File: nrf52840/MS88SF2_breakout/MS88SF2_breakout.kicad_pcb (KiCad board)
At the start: 2 copper layers, 1 part, among them U1 MS88SF2

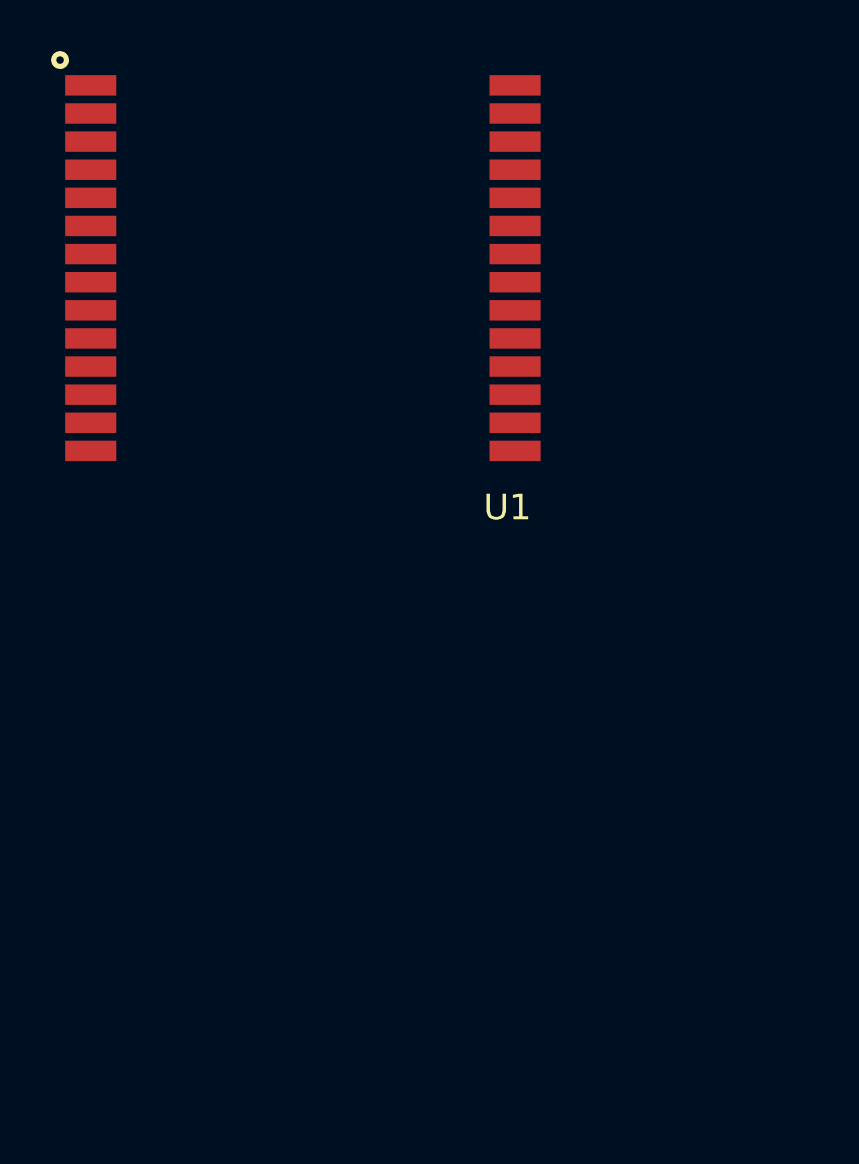
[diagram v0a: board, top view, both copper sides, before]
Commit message: nrf5: Start routing
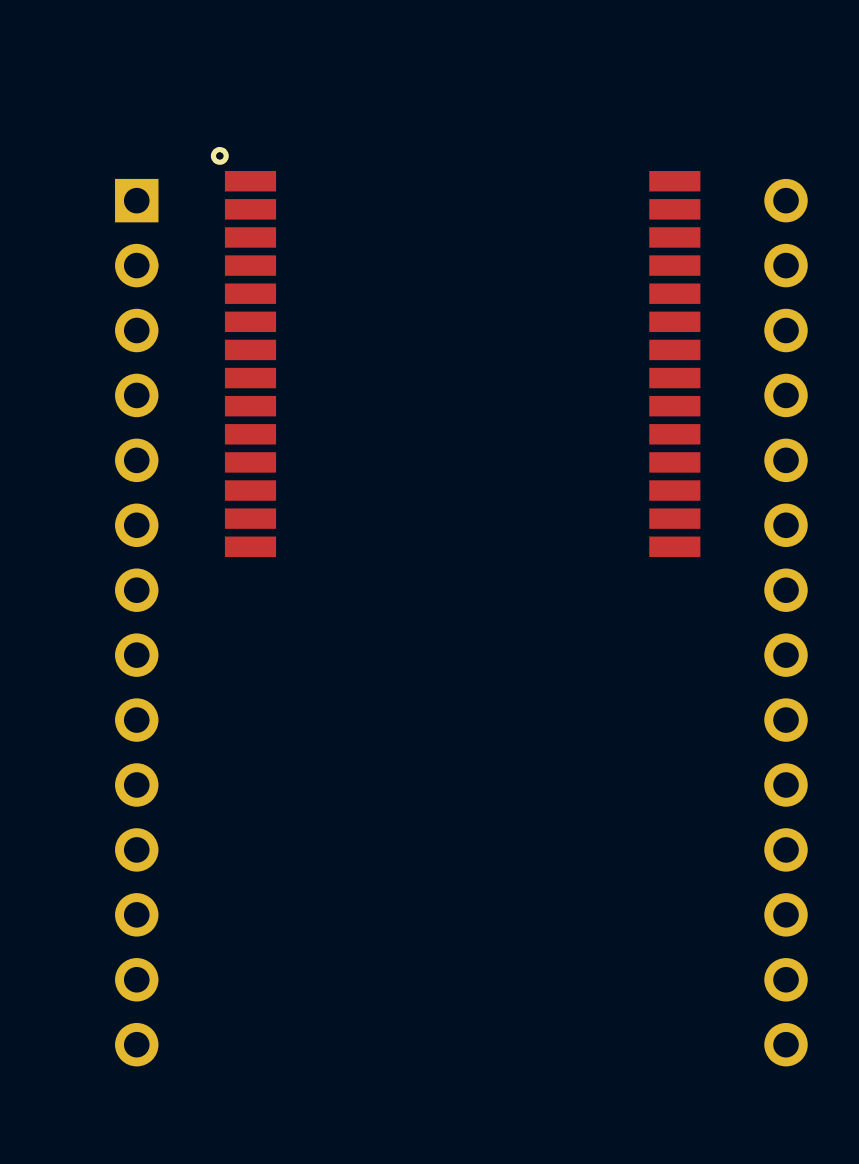
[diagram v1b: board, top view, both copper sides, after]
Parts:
- added J1: Conn_01x14_Male, !myfoots:PinHeader_1x14_P2.54mm_Vertical, F.Cu at (63.0, 60.0)
- added J2: Conn_01x14_Male, !myfoots:PinHeader_1x14_P2.54mm_Vertical_2row, F.Cu at (88.4, 60.0)
- moved U1 7.29 mm to (75.8, 63.2)
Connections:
- U1 pad 10: (no net) -> P0.08
- U1 pad 11: (no net) -> P1.09
- U1 pad 12: (no net) -> P0.12
- U1 pad 18: (no net) -> P0.13
- U1 pad 19: (no net) -> P0.15
- U1 pad 2: (no net) -> P1.13
- U1 pad 20: (no net) -> P0.18
- U1 pad 21: (no net) -> P0.20
- U1 pad 22: (no net) -> P0.22
- U1 pad 23: (no net) -> P0.24
- U1 pad 24: (no net) -> P1.00
- U1 pad 25: (no net) -> SWDIO
- U1 pad 26: (no net) -> SWCLK
- U1 pad 27: (no net) -> P0.09
- U1 pad 28: (no net) -> P0.10
- U1 pad 3: (no net) -> P1.15
- U1 pad 4: (no net) -> P0.02
- U1 pad 5: (no net) -> P0.29
- U1 pad 6: (no net) -> P0.31
- U1 pad 7: (no net) -> P0.26
- U1 pad 8: (no net) -> P0.04
- U1 pad 9: (no net) -> P0.06

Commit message: nrf5: Prepare for routing
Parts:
- moved U1 8.75 mm to (75.7, 72.0)
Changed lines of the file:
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@@
     (thickness 1.6)
     (drawings 0)
-    (tracks 1)
+    (tracks 0)
     (zones 0)
     (modules 3)
@@
     (47 F.CrtYd user)
     (48 B.Fab user)
-    (49 F.Fab user hide)
+    (49 F.Fab user)
   )
   (setup
-    (last_trace_width 0.8)
+    (last_trace_width 0.4)
     (user_trace_width 0.4)
     (user_trace_width 0.8)
@@
   )
   (module MS88SF2:MS88SF2 (layer F.Cu)
-    (at 75.75 63.25)
+    (at 75.7 72)
     (fp_text reference U1 (at 8 12.5) (layer F.Fab)
       (effects (font (size 1 1) (thickness 0.15)))
@@
       (effects (font (size 1 1) (thickness 0.15)))
     )
+    (fp_line (start -12.7 -5.81) (end 12.7 -17.6) (layer F.Fab) (width 0.12))
+    (fp_line (start 12.7 -5.81) (end -12.7 -17.6) (layer F.Fab) (width 0.12))
+    (fp_circle (center -9.5 -5) (end -9.4 -5) (layer F.SilkS) (width 0.5))
+    (fp_line (start 12.7 -17.6) (end -12.7 -17.6) (layer F.Fab) (width 0.12))
+    (fp_line (start 8.7 -5.81) (end -8.7 -5.81) (layer F.Fab) (width 0.12))
+    (fp_line (start 12.7 -5.81) (end 12.7 -17.6) (layer F.Fab) (width 0.12))
+    (fp_line (start 8.7 -5.81) (end 12.7 -5.81) (layer F.Fab) (width 0.12))
+    (fp_line (start -12.7 -5.81) (end -12.7 -17.6) (layer F.Fab) (width 0.12))
+    (fp_line (start -8.7 -5.81) (end -12.7 -5.81) (layer F.Fab) (width 0.12))
+    (fp_line (start 8.7 11.6) (end 8.7 -11.6) (layer F.Fab) (width 0.12))
+    (fp_line (start -8.7 11.6) (end 8.7 11.6) (layer F.Fab) (width 0.12))
+    (fp_line (start -8.7 -11.6) (end -8.7 11.6) (layer F.Fab) (width 0.12))
+    (fp_line (start 8.7 -11.6) (end -8.7 -11.6) (layer F.Fab) (width 0.12))
     (fp_text user "No copper" (at 0 -16) (layer F.Fab)
       (effects (font (size 1 1) (thickness 0.15)))
     )
-    (fp_line (start 8.7 -11.6) (end -8.7 -11.6) (layer F.Fab) (width 0.12))
-    (fp_line (start -8.7 -11.6) (end -8.7 11.6) (layer F.Fab) (width 0.12))
-    (fp_line (start -8.7 11.6) (end 8.7 11.6) (layer F.Fab) (width 0.12))
-    (fp_line (start 8.7 11.6) (end 8.7 -11.6) (layer F.Fab) (width 0.12))
-    (fp_line (start -8.7 -5.81) (end -12.7 -5.81) (layer F.Fab) (width 0.12))
-    (fp_line (start -12.7 -5.81) (end -12.7 -17.6) (layer F.Fab) (width 0.12))
-    (fp_line (start 8.7 -5.81) (end 12.7 -5.81) (layer F.Fab) (width 0.12))
-    (fp_line (start 12.7 -5.81) (end 12.7 -17.6) (layer F.Fab) (width 0.12))
-    (fp_line (start 8.7 -5.81) (end -8.7 -5.81) (layer F.Fab) (width 0.12))
-    (fp_line (start 12.7 -17.6) (end -12.7 -17.6) (layer F.Fab) (width 0.12))
-    (fp_circle (center -9.5 -5) (end -9.4 -5) (layer F.SilkS) (width 0.5))
-    (fp_line (start 12.7 -5.81) (end -12.7 -17.6) (layer F.Fab) (width 0.12))
-    (fp_line (start -12.7 -5.81) (end 12.7 -17.6) (layer F.Fab) (width 0.12))
     (pad 1 smd rect (at -8.3 -4.01) (size 2 0.8) (layers F.Cu F.Paste F.Mask)
       (net 2 GND))
@@
       (effects (font (size 1 1) (thickness 0.15)))
     )
+    (fp_line (start -1.27 -0.635) (end -0.635 -1.27) (layer F.Fab) (width 0.1))
+    (fp_line (start -1.27 34.29) (end -1.27 -0.635) (layer F.Fab) (width 0.1))
+    (fp_line (start 1.27 34.29) (end -1.27 34.29) (layer F.Fab) (width 0.1))
+    (fp_line (start 1.27 -1.27) (end 1.27 34.29) (layer F.Fab) (width 0.1))
+    (fp_line (start -0.635 -1.27) (end 1.27 -1.27) (layer F.Fab) (width 0.1))
     (fp_text user %R (at 0 16.51 90) (layer F.Fab)
       (effects (font (size 1 1) (thickness 0.15)))
     )
-    (fp_line (start -0.635 -1.27) (end 1.27 -1.27) (layer F.Fab) (width 0.1))
-    (fp_line (start 1.27 -1.27) (end 1.27 34.29) (layer F.Fab) (width 0.1))
-    (fp_line (start 1.27 34.29) (end -1.27 34.29) (layer F.Fab) (width 0.1))
-    (fp_line (start -1.27 34.29) (end -1.27 -0.635) (layer F.Fab) (width 0.1))
-    (fp_line (start -1.27 -0.635) (end -0.635 -1.27) (layer F.Fab) (width 0.1))
     (pad 14 thru_hole oval (at 0 33.02) (size 1.7 1.7) (drill 1) (layers *.Cu *.Mask)
       (net 1 +3V3))
@@
       (effects (font (size 1 1) (thickness 0.15)))
     )
+    (fp_line (start -0.635 -1.27) (end 1.27 -1.27) (layer F.Fab) (width 0.1))
+    (fp_line (start 1.27 -1.27) (end 1.27 34.29) (layer F.Fab) (width 0.1))
+    (fp_line (start 1.27 34.29) (end -1.27 34.29) (layer F.Fab) (width 0.1))
+    (fp_line (start -1.27 34.29) (end -1.27 -0.635) (layer F.Fab) (width 0.1))
+    (fp_line (start -1.27 -0.635) (end -0.635 -1.27) (layer F.Fab) (width 0.1))
     (fp_text user %R (at 0 16.51 90) (layer F.Fab)
       (effects (font (size 1 1) (thickness 0.15)))
     )
-    (fp_line (start -1.27 -0.635) (end -0.635 -1.27) (layer F.Fab) (width 0.1))
-    (fp_line (start -1.27 34.29) (end -1.27 -0.635) (layer F.Fab) (width 0.1))
-    (fp_line (start 1.27 34.29) (end -1.27 34.29) (layer F.Fab) (width 0.1))
-    (fp_line (start 1.27 -1.27) (end 1.27 34.29) (layer F.Fab) (width 0.1))
-    (fp_line (start -0.635 -1.27) (end 1.27 -1.27) (layer F.Fab) (width 0.1))
     (pad 15 thru_hole oval (at 0 33.02) (size 1.7 1.7) (drill 1) (layers *.Cu *.Mask))
     (pad 16 thru_hole oval (at 0 30.48) (size 1.7 1.7) (drill 1) (layers *.Cu *.Mask))
@@
     )
   )
-  (segment (start 63.45 62.54) (end 63 62.54) (width 0.8) (layer F.Cu) (net 24))
 )

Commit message: nrf5: Adjust position
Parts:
- moved U1 7.54 mm to (74.4, 64.6)
- moved J2 2.54 mm to (85.9, 60.0)
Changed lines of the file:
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@@
   )
   (setup
-    (last_trace_width 0.4)
+    (last_trace_width 0.25)
     (user_trace_width 0.4)
     (user_trace_width 0.8)
@@
   )
   (module MS88SF2:MS88SF2 (layer F.Cu)
-    (at 75.7 72)
+    (at 74.43 64.572)
     (fp_text reference U1 (at 8 12.5) (layer F.Fab)
       (effects (font (size 1 1) (thickness 0.15)))
@@
       (effects (font (size 1 1) (thickness 0.15)))
     )
+    (fp_line (start 8.7 -11.6) (end -8.7 -11.6) (layer F.Fab) (width 0.12))
+    (fp_line (start -8.7 -11.6) (end -8.7 11.6) (layer F.Fab) (width 0.12))
+    (fp_line (start -8.7 11.6) (end 8.7 11.6) (layer F.Fab) (width 0.12))
+    (fp_line (start 8.7 11.6) (end 8.7 -11.6) (layer F.Fab) (width 0.12))
+    (fp_line (start -8.7 -5.81) (end -12.7 -5.81) (layer F.Fab) (width 0.12))
+    (fp_line (start -12.7 -5.81) (end -12.7 -17.6) (layer F.Fab) (width 0.12))
+    (fp_line (start 8.7 -5.81) (end 12.7 -5.81) (layer F.Fab) (width 0.12))
+    (fp_line (start 12.7 -5.81) (end 12.7 -17.6) (layer F.Fab) (width 0.12))
+    (fp_line (start 8.7 -5.81) (end -8.7 -5.81) (layer F.Fab) (width 0.12))
+    (fp_line (start 12.7 -17.6) (end -12.7 -17.6) (layer F.Fab) (width 0.12))
+    (fp_circle (center -9.5 -5) (end -9.4 -5) (layer F.SilkS) (width 0.5))
+    (fp_line (start 12.7 -5.81) (end -12.7 -17.6) (layer F.Fab) (width 0.12))
     (fp_line (start -12.7 -5.81) (end 12.7 -17.6) (layer F.Fab) (width 0.12))
-    (fp_line (start 12.7 -5.81) (end -12.7 -17.6) (layer F.Fab) (width 0.12))
-    (fp_circle (center -9.5 -5) (end -9.4 -5) (layer F.SilkS) (width 0.5))
-    (fp_line (start 12.7 -17.6) (end -12.7 -17.6) (layer F.Fab) (width 0.12))
-    (fp_line (start 8.7 -5.81) (end -8.7 -5.81) (layer F.Fab) (width 0.12))
-    (fp_line (start 12.7 -5.81) (end 12.7 -17.6) (layer F.Fab) (width 0.12))
-    (fp_line (start 8.7 -5.81) (end 12.7 -5.81) (layer F.Fab) (width 0.12))
-    (fp_line (start -12.7 -5.81) (end -12.7 -17.6) (layer F.Fab) (width 0.12))
-    (fp_line (start -8.7 -5.81) (end -12.7 -5.81) (layer F.Fab) (width 0.12))
-    (fp_line (start 8.7 11.6) (end 8.7 -11.6) (layer F.Fab) (width 0.12))
-    (fp_line (start -8.7 11.6) (end 8.7 11.6) (layer F.Fab) (width 0.12))
-    (fp_line (start -8.7 -11.6) (end -8.7 11.6) (layer F.Fab) (width 0.12))
-    (fp_line (start 8.7 -11.6) (end -8.7 -11.6) (layer F.Fab) (width 0.12))
     (fp_text user "No copper" (at 0 -16) (layer F.Fab)
       (effects (font (size 1 1) (thickness 0.15)))
@@
       (net 3 P0.10))
   )
-  (module !myfoots:PinHeader_1x14_P2.54mm_Vertical locked (layer F.Cu)
+  (module !myfoots:PinHeader_1x14_P2.54mm_Vertical (layer F.Cu)
     (at 63 60)
     (descr "Through hole straight pin header, 1x14, 2.54mm pitch, single row")
@@
       (effects (font (size 1 1) (thickness 0.15)))
     )
+    (fp_line (start -0.635 -1.27) (end 1.27 -1.27) (layer F.Fab) (width 0.1))
+    (fp_line (start 1.27 -1.27) (end 1.27 34.29) (layer F.Fab) (width 0.1))
+    (fp_line (start 1.27 34.29) (end -1.27 34.29) (layer F.Fab) (width 0.1))
+    (fp_line (start -1.27 34.29) (end -1.27 -0.635) (layer F.Fab) (width 0.1))
     (fp_line (start -1.27 -0.635) (end -0.635 -1.27) (layer F.Fab) (width 0.1))
-    (fp_line (start -1.27 34.29) (end -1.27 -0.635) (layer F.Fab) (width 0.1))
-    (fp_line (start 1.27 34.29) (end -1.27 34.29) (layer F.Fab) (width 0.1))
-    (fp_line (start 1.27 -1.27) (end 1.27 34.29) (layer F.Fab) (width 0.1))
-    (fp_line (start -0.635 -1.27) (end 1.27 -1.27) (layer F.Fab) (width 0.1))
     (fp_text user %R (at 0 16.51 90) (layer F.Fab)
       (effects (font (size 1 1) (thickness 0.15)))
@@
     )
   )
-  (module !myfoots:PinHeader_1x14_P2.54mm_Vertical_2row locked (layer F.Cu)
-    (at 88.4 60)
+  (module !myfoots:PinHeader_1x14_P2.54mm_Vertical_2row (layer F.Cu)
+    (at 85.86 60)
     (descr "Through hole straight pin header, 1x14, 2.54mm pitch, single row")
     (tags "Through hole pin header THT 1x14 2.54mm single row")
@@
       (effects (font (size 1 1) (thickness 0.15)))
     )
+    (fp_line (start -1.27 -0.635) (end -0.635 -1.27) (layer F.Fab) (width 0.1))
+    (fp_line (start -1.27 34.29) (end -1.27 -0.635) (layer F.Fab) (width 0.1))
+    (fp_line (start 1.27 34.29) (end -1.27 34.29) (layer F.Fab) (width 0.1))
+    (fp_line (start 1.27 -1.27) (end 1.27 34.29) (layer F.Fab) (width 0.1))
     (fp_line (start -0.635 -1.27) (end 1.27 -1.27) (layer F.Fab) (width 0.1))
-    (fp_line (start 1.27 -1.27) (end 1.27 34.29) (layer F.Fab) (width 0.1))
-    (fp_line (start 1.27 34.29) (end -1.27 34.29) (layer F.Fab) (width 0.1))
-    (fp_line (start -1.27 34.29) (end -1.27 -0.635) (layer F.Fab) (width 0.1))
-    (fp_line (start -1.27 -0.635) (end -0.635 -1.27) (layer F.Fab) (width 0.1))
     (fp_text user %R (at 0 16.51 90) (layer F.Fab)
       (effects (font (size 1 1) (thickness 0.15)))

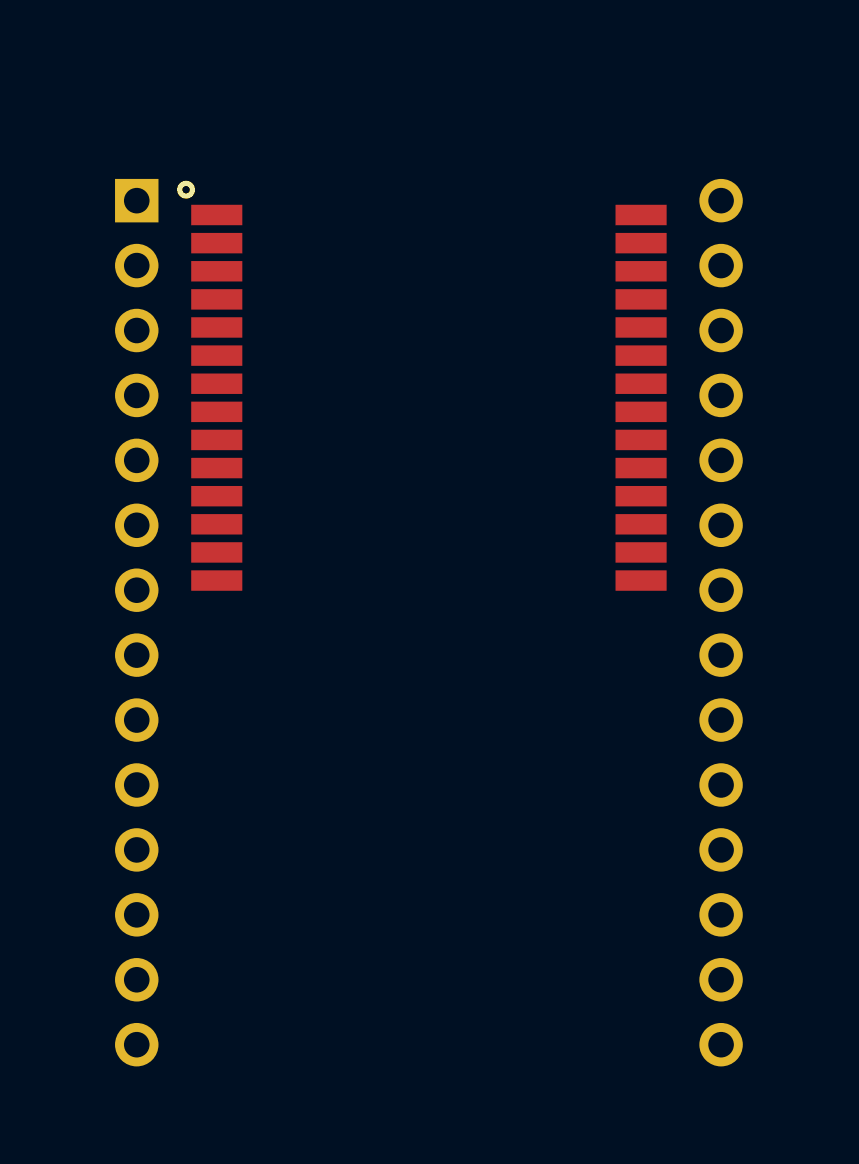
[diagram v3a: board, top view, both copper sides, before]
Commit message: nrf5: Routing done
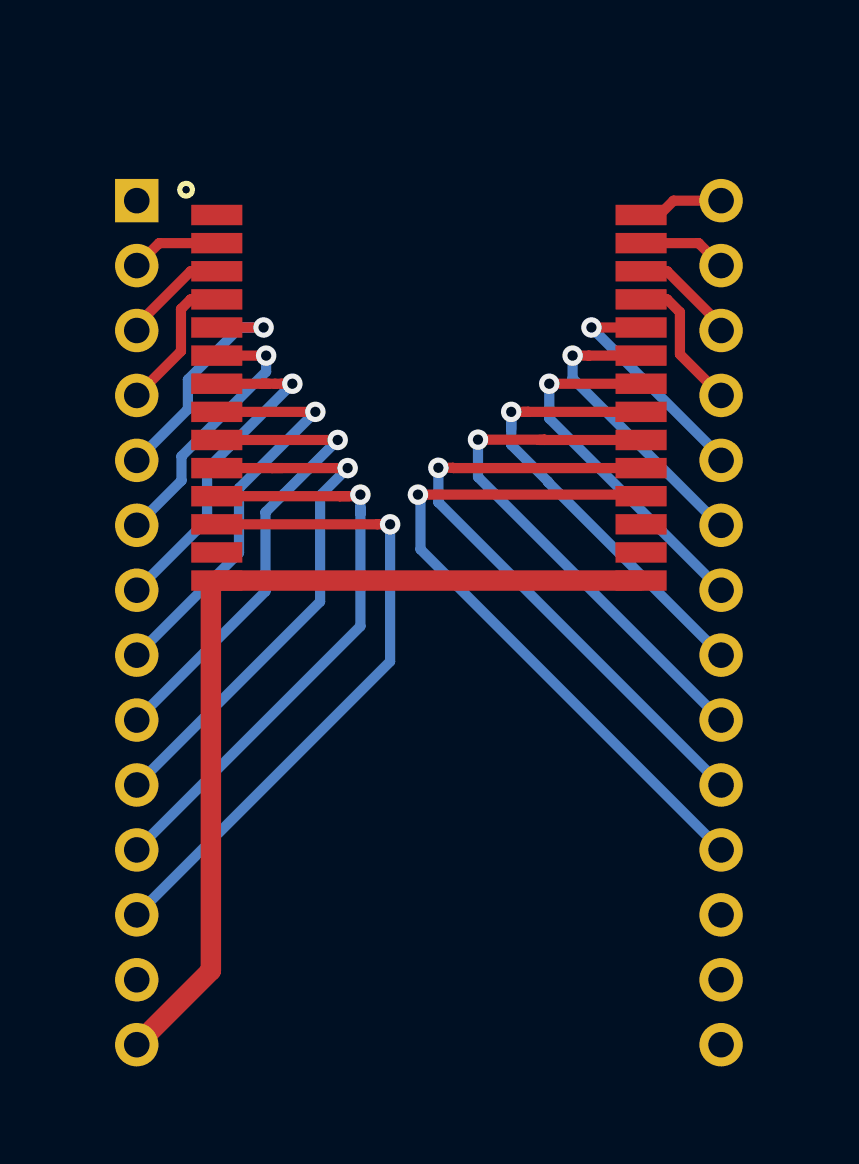
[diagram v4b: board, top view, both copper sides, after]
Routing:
- net +3V3: track 0.00 -> 36.1 mm
- net P0.13: track 0.00 -> 27.3 mm, vias 0 -> 1
- net P0.12: track 0.00 -> 26.2 mm, vias 0 -> 1
- net P0.15: track 0.00 -> 24.9 mm, vias 0 -> 1
- net P1.09: track 0.00 -> 23.8 mm, vias 0 -> 1
- net P0.18: track 0.00 -> 21.5 mm, vias 0 -> 1
- net P0.08: track 0.00 -> 21.4 mm, vias 0 -> 1
- net P0.06: track 0.00 -> 18.9 mm, vias 0 -> 1
- net P0.20: track 0.00 -> 18.9 mm, vias 0 -> 1
- net P0.04: track 0.00 -> 16.3 mm, vias 0 -> 1
- net P0.22: track 0.00 -> 14.5 mm, vias 0 -> 1
- net P0.26: track 0.00 -> 13.9 mm, vias 0 -> 1
- net P0.24: track 0.00 -> 11.8 mm, vias 0 -> 1
- net P0.31: track 0.00 -> 10.7 mm, vias 0 -> 1
- net P0.29: track 0.00 -> 9.63 mm, vias 0 -> 1
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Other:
- rule trace_min: 0.2 -> 0.25
